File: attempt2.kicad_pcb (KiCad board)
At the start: 4 copper layers, 71.5 x 54.4 mm, 57 parts, among them J3 Conn_02x05_Pin, J4 USB_C_Receptacle_USB2.0_14P, J5 SIM_Card, SW1 SW_Push, SW4 SW_Push, U3 MCP73831T-2ACI_OT, U4 NRF9151-LACA-R7, U5 MAX2686LEWS_, U6 TPD3F303DPVR, U7 CP2102N-A02-GQFN24R

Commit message: changed literally everything moved so much.
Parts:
- removed J3: Conn_02x05_Pin, Connector_PinSocket_2.54mm:PinSocket_2x05_P2.54mm_Vertical_SMD
- removed JP2: SolderJumper_Open, Jumper:SolderJumper-2_P1.3mm_Open_RoundedPad1.0x1.5mm
- removed TP20: TestPoint, TestPoint:TestPoint_Pad_D2.0mm
- removed U6: TPD3F303DPVR, TPD3F303DPVR:SON50P210X160X65-9N
- added D2: LED, LED_SMD:LED_1206_3216Metric, F.Cu at (119.9, 112.1)
- added D4: LED, LED_SMD:LED_1206_3216Metric, F.Cu at (122.5, 131.8)
- added D5: LED, LED_SMD:LED_1206_3216Metric, F.Cu at (122.7, 126.5)
- added D6: LED, LED_SMD:LED_1206_3216Metric, F.Cu at (122.7, 129.1)
- added J1: Conn_ARM_JTAG_SWD_10, Connector_PinSocket_2.54mm:PinSocket_2x05_P2.54mm_Vertical_SMD, F.Cu at (155.0, 135.5)
- added R1: 2k, Resistor_SMD:R_0603_1608Metric, F.Cu at (119.4, 114.6)
- added R9: 2k, Resistor_SMD:R_0603_1608Metric, F.Cu at (118.5, 129.1)
- C8: value 100nF -> 10p
- C9: value 10p -> 100n
- R7, R8: value 50 -> 2k
- moved R10 22.2 mm to (146.4, 133.8), turned to -90 degrees
- moved TP6 19.2 mm to (142.7, 137.1)
- moved R7 16.5 mm to (118.5, 131.8), turned to 0 degrees
- moved R8 14.4 mm to (118.7, 126.5), turned to 0 degrees
- moved E1 13.2 mm to (99.9, 119.6)
- moved L1 12.8 mm to (112.9, 118.6), turned to 180 degrees
- moved D3 12.7 mm to (141.8, 132.3), turned to -90 degrees
- moved C8 11.3 mm to (116.4, 118.6), turned to 0 degrees
- moved U5 10.7 mm to (119.6, 118.8), turned to -90 degrees
- moved R11 10.1 mm to (133.3, 132.3), turned to -90 degrees
- moved SW1 8.40 mm to (137.1, 137.8)
- moved C23 8.12 mm to (135.4, 132.4), turned to -90 degrees
- moved C22 8.02 mm to (137.0, 132.4), turned to -90 degrees
- moved D1 7.68 mm to (130.7, 131.8), turned to -90 degrees
- moved C25 6.67 mm to (150.4, 118.7)
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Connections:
- FL1 pad C: COEX0 -> Net-(FL1-IN)
- R5 pad 1: Net-(JP2-A) -> +3V8
- R6 pad 1: COEX0 -> Net-(FL1-IN)
- R6 pad 2: GND -> LNA_ENABLE
- R7 pad 1: COEX0 -> +3V8
- R7 pad 2: GND -> Net-(D4-A)
- R8 pad 1: GPS -> +3V8
- R8 pad 2: GND -> Net-(D5-A)
- TP10 pad 1: Net-(U3-STAT) -> CHARGE_STAT
- U3 pad 1: Net-(U3-STAT) -> CHARGE_STAT
- U4 pad 1: (no net) -> GND
- U4 pad 105: (no net) -> GND
- U4 pad 106: (no net) -> GND
- U4 pad 107: (no net) -> GND
- U4 pad 108: (no net) -> GND
- U4 pad 109: (no net) -> GND
- U4 pad 110: (no net) -> GND
- U4 pad 111: (no net) -> GND
- U4 pad 112: (no net) -> GND
- U4 pad 113: (no net) -> GND
- U4 pad 13: (no net) -> GND
- U4 pad 15: (no net) -> GND
- U4 pad 16: Net-(U4A-SIM_RST) -> Net-(J5-RST)
- U4 pad 17: Net-(U4A-SIM_IO) -> Net-(J5-I/O)
- U4 pad 18: Net-(U4A-SIM_CLK) -> Net-(J5-CLK)
- U4 pad 20: (no net) -> GND
- U4 pad 25: (no net) -> GND
- U4 pad 30: (no net) -> GND
- U4 pad 34: (no net) -> GND
- U4 pad 38: (no net) -> GND
- U4 pad 39: (no net) -> GND
- U4 pad 40: (no net) -> GND
- U4 pad 41: (no net) -> GND
- U4 pad 43: (no net) -> GND
- U4 pad 46: (no net) -> GND
- U4 pad 48: unconnected-(U4A-P0.29-Pad48) -> CHARGE_STAT
- U4 pad 51: (no net) -> GND
- U4 pad 52: COEX0 -> LNA_ENABLE
- U4 pad 55: (no net) -> GND
- U4 pad 57: unconnected-(U4A-P0.01-Pad57) -> LED_3
- U4 pad 58: unconnected-(U4A-P0.02-Pad58) -> LED_2
- U4 pad 59: unconnected-(U4A-P0.03-Pad59) -> LED_1
- U4 pad 60: (no net) -> GND
- U4 pad 66: (no net) -> GND
- U4 pad 7: (no net) -> GND
- U4 pad 71: (no net) -> GND
- U4 pad 76: (no net) -> GND
- U5 pad A2: COEX0 -> Net-(FL1-IN)
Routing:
- net CHARGE_STAT: track 0.00 -> 30.9 mm, vias 0 -> 2
- net GND: track 9.03 -> 35.4 mm, vias 47 -> 74
- net Net-(J1-~{RESET}): track 27.0 -> 3.47 mm
- net +3V8: track 88.7 -> 105.8 mm, vias 7 -> 8
- net STATUS_LED: track 20.4 -> 4.60 mm, vias 2 -> 0
- net COEX0: track 14.9 -> 0.00 mm
- net LNA_ENABLE: track 0.00 -> 11.1 mm
- net LED_1: track 0.00 -> 10.7 mm
- net Net-(FL1-IN): track 0.00 -> 10.3 mm
- net LED_2: track 0.00 -> 9.62 mm
- net Net-(J5-VCC): track 23.6 -> 14.5 mm, vias 0 -> 2
- net Net-(J5-CLK): track 4.08 -> 13.0 mm
- net Net-(J5-RST): track 3.51 -> 12.2 mm
- net LED_3: track 0.00 -> 8.70 mm
- net Net-(J5-I/O): track 4.40 -> 13.0 mm, vias 0 -> 2
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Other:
- board size 71.5 x 54.4 mm -> 88.5 x 54.4 mm

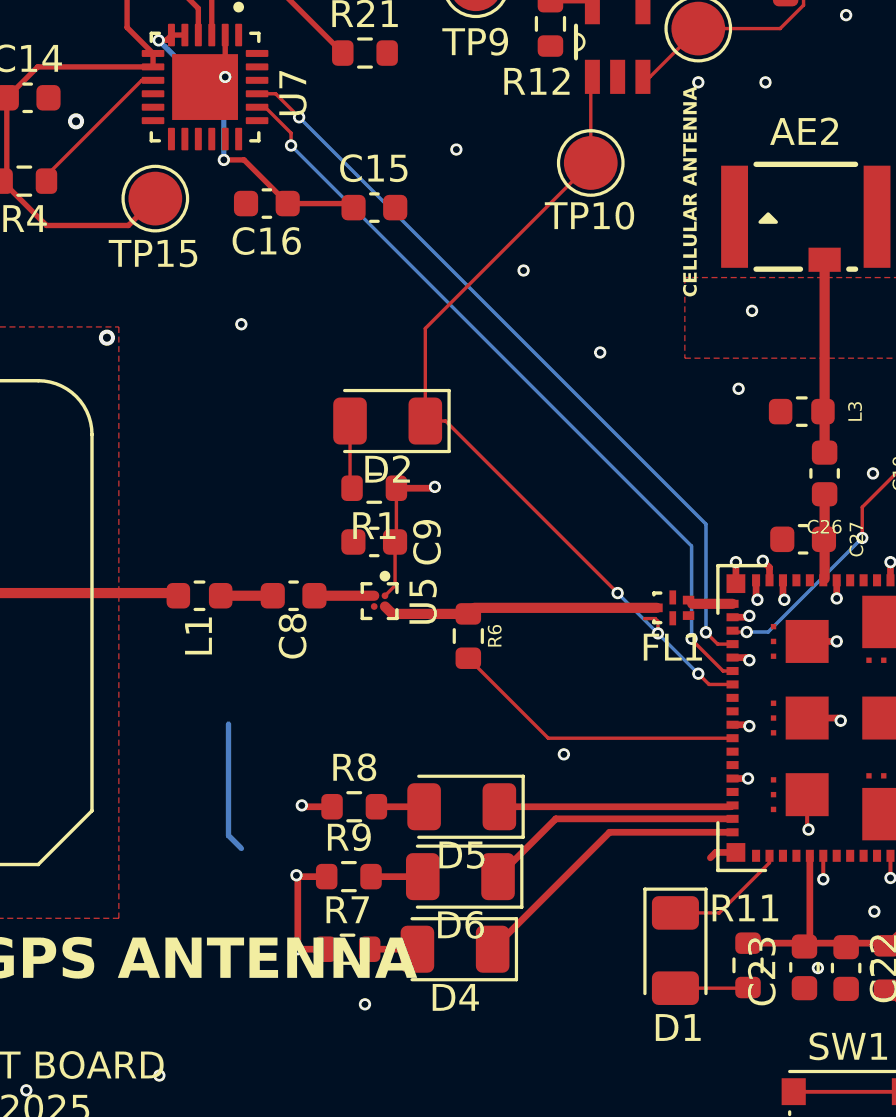
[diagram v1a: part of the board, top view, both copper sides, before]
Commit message: added more netclass vals
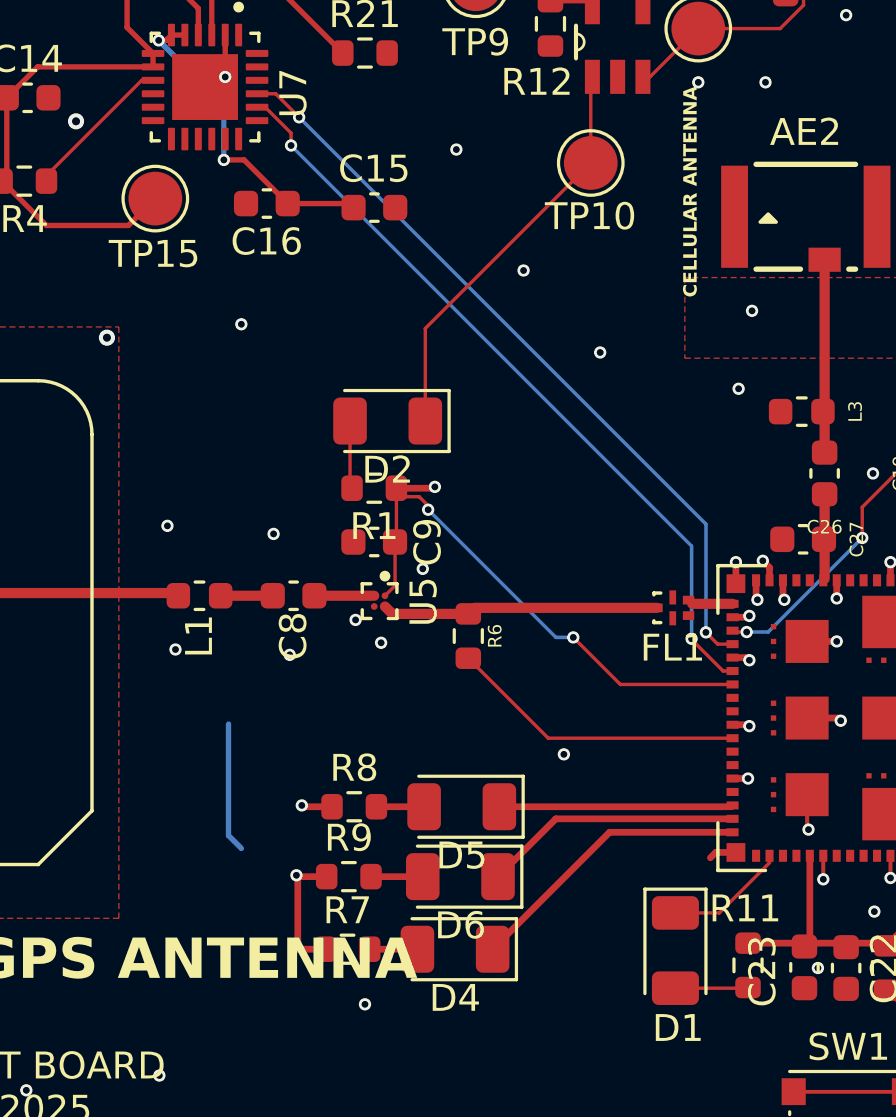
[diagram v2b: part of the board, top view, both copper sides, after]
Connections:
- D2 pad 1: CHARGE_STAT -> Net-(D2-K)
- R1 pad 1: +3V8 -> CHARGE_STAT
- TP10 pad 1: CHARGE_STAT -> Net-(D2-K)
- U3 pad 1: CHARGE_STAT -> Net-(D2-K)
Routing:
- net CHARGE_STAT: track 30.9 -> 15.2 mm
- net Net-(D2-K): track 0.00 -> 15.1 mm
- net GND: track 35.4 -> 34.4 mm, vias 74 -> 80
- net +3V8: vias 8 -> 7
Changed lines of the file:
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@@
 	(net 91 "+3V8")
 	(net 92 "Net-(E1-Pad1)")
+	(net 93 "Net-(D2-K)")
 	(footprint "Resistor_SMD:R_0603_1608Metric"
 		(layer "F.Cu")
@@
 			(size 2 2)
 			(layers "F.Cu" "F.Mask")
-			(net 14 "CHARGE_STAT")
+			(net 93 "Net-(D2-K)")
 			(pinfunction "1")
 			(pintype "passive")
@@
 			(layers "F.Cu" "F.Mask" "F.Paste")
 			(roundrect_rratio 0.2)
-			(net 14 "CHARGE_STAT")
+			(net 93 "Net-(D2-K)")
 			(pinfunction "K")
 			(pintype "passive")
@@
 			(layers "F.Cu" "F.Mask" "F.Paste")
 			(roundrect_rratio 0.25)
-			(net 91 "+3V8")
+			(net 14 "CHARGE_STAT")
 			(pintype "passive")
 		)
@@
 			(size 1.27 0.5588)
 			(layers "F.Cu" "F.Mask" "F.Paste")
-			(net 14 "CHARGE_STAT")
+			(net 93 "Net-(D2-K)")
 			(pinfunction "STAT")
 			(pintype "output")
@@
 	)
 	(segment
-		(start 130 120)
-		(end 130 119.5526)
-		(width 0.127)
-		(layer "F.Cu")
-		(net 1)
-	)
-	(segment
-		(start 129.8974 119.45)
-		(end 129.5 119.45)
-		(width 0.127)
-		(layer "F.Cu")
-		(net 1)
-	)
-	(segment
 		(start 133.65 118.7)
 		(end 133.7 118.75)
@@
 	)
 	(segment
-		(start 130 119.5526)
-		(end 129.8974 119.45)
-		(width 0.127)
-		(layer "F.Cu")
-		(net 1)
-	)
-	(segment
 		(start 139.575 119.575)
 		(end 139.6 119.6)
@@
 	)
 	(via
+		(at 115.7 116.3)
+		(size 0.4572)
+		(drill 0.254)
+		(layers "F.Cu" "B.Cu")
+		(free yes)
+		(net 1)
+	)
+	(via
 		(at 128.5 92)
 		(size 0.4572)
@@
 	)
 	(via
+		(at 119.7 120.35)
+		(size 0.4572)
+		(drill 0.254)
+		(layers "F.Cu" "B.Cu")
+		(free yes)
+		(net 1)
+	)
+	(via
 		(at 167.5 110.05)
 		(size 0.4572)
@@
 	)
 	(via
+		(at 111.75 116)
+		(size 0.4572)
+		(drill 0.254)
+		(layers "F.Cu" "B.Cu")
+		(free yes)
+		(net 1)
+	)
+	(via
 		(at 141.25 124.4)
 		(size 0.4572)
@@
 	)
 	(via
+		(at 112.05 120.6)
+		(size 0.4572)
+		(drill 0.254)
+		(layers "F.Cu" "B.Cu")
+		(free yes)
+		(net 1)
+	)
+	(via
 		(at 138.05 130.35)
 		(size 0.4572)
@@
 	)
 	(via
+		(at 118.75 119.5)
+		(size 0.4572)
+		(drill 0.254)
+		(layers "F.Cu" "B.Cu")
+		(free yes)
+		(net 1)
+	)
+	(via
 		(at 133.4 123.45)
 		(size 0.4572)
@@
 	)
 	(via
+		(at 116.3 120.8)
+		(size 0.4572)
+		(drill 0.254)
+		(layers "F.Cu" "B.Cu")
+		(free yes)
+		(net 1)
+	)
+	(via
 		(at 139.45 126.75)
 		(size 0.4572)
@@
 		(net 1)
 	)
-	(via blind
-		(at 130 120)
-		(size 0.4572)
-		(drill 0.254)
-		(layers "F.Cu" "In2.Cu")
-		(net 1)
-	)
 	(via
 		(at 154 100.05)
@@
 	)
 	(via
+		(at 121.25 117.6)
+		(size 0.4572)
+		(drill 0.254)
+		(layers "F.Cu" "B.Cu")
+		(free yes)
+		(net 1)
+	)
+	(via
 		(at 111.45 136.45)
 		(size 0.4572)
@@
 	)
 	(segment
-		(start 121.34375 108.65625)
-		(end 127.5 102.5)
-		(width 0.127)
-		(layer "F.Cu")
-		(net 14)
-	)
-	(segment
-		(start 127.5 102.5)
-		(end 127.5 99.3556)
-		(width 0.127)
-		(layer "F.Cu")
-		(net 14)
-	)
-	(segment
-		(start 121.34375 112.1)
-		(end 121.34375 108.65625)
-		(width 0.127)
-		(layer "F.Cu")
-		(net 14)
-	)
-	(segment
-		(start 127.5 99.3556)
-		(end 127.5602 99.2954)
+		(start 121.45 115.25)
+		(end 121.1165 114.9165)
 		(width 0.127)
 		(layer "F.Cu")
@@
 	)
 	(segment
-		(start 122.1 112.1)
-		(end 128.5 118.5)
+		(start 132.775 121.9)
+		(end 128.6 121.9)
 		(width 0.127)
 		(layer "F.Cu")
@@
 	)
 	(segment
-		(start 121.34375 112.1)
-		(end 122.1 112.1)
+		(start 121.1165 114.9165)
+		(end 120.52375 114.9165)
 		(width 0.127)
 		(layer "F.Cu")
@@
 	)
 	(segment
-		(start 131.9 121.9)
-		(end 132.775 121.9)
+		(start 121.45 115.4)
+		(end 121.45 115.25)
 		(width 0.127)
 		(layer "F.Cu")
@@
 	)
 	(segment
-		(start 131.5 121.5)
-		(end 131.9 121.9)
+		(start 128.6 121.9)
+		(end 126.85 120.15)
 		(width 0.127)
 		(layer "F.Cu")
@@
 	)
 	(via
-		(at 128.5 118.5)
+		(at 121.45 115.4)
 		(size 0.4572)
 		(drill 0.254)
@@
 	)
 	(via
-		(at 131.5 121.5)
+		(at 126.85 120.15)
 		(size 0.4572)
 		(drill 0.254)
@@
 	)
 	(segment
-		(start 128.5 118.5)
-		(end 131.5 121.5)
+		(start 126.85 120.15)
+		(end 126.2 120.15)
+		(width 0.127)
+		(layer "B.Cu")
+		(net 14)
+	)
+	(segment
+		(start 126.2 120.15)
+		(end 121.45 115.4)
 		(width 0.127)
 		(layer "B.Cu")
@@
 	)
 	(via
-		(at 116.6 131.75)
-		(size 0.4572)
-		(drill 0.254)
-		(layers "F.Cu" "B.Cu")
-		(net 91)
-	)
-	(via
 		(at 149.65 127.3309)
 		(size 0.4572)
@@
 		(net 92)
 	)
+	(segment
+		(start 127.5 102.5)
+		(end 121.34375 108.65625)
+		(width 0.127)
+		(layer "F.Cu")
+		(net 93)
+	)
+	(segment
+		(start 127.5 102.5)
+		(end 127.5 99.3556)
+		(width 0.127)
+		(layer "F.Cu")
+		(net 93)
+	)
+	(segment
+		(start 127.5 99.3556)
+		(end 127.5602 99.2954)
+		(width 0.127)
+		(layer "F.Cu")
+		(net 93)
+	)
+	(segment
+		(start 121.34375 108.65625)
+		(end 121.34375 111.845)
+		(width 0.127)
+		(layer "F.Cu")
+		(net 93)
+	)
 	(zone
